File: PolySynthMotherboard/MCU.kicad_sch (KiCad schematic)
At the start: 45 parts, among them J201 SWD Header, J202 USB_C, J203 MIDI_In, J204 MIDI_Thru, J207 MIDI_Out, J401 Micro_SD_Card_Det2, SW201 RST, SW202 BOOT, U201 STM32F411RETx, U202 74HC595, U203 74HC595, U204 4N35, U205 74HC04, Y201 16MHz, Y202 32.768kHZ

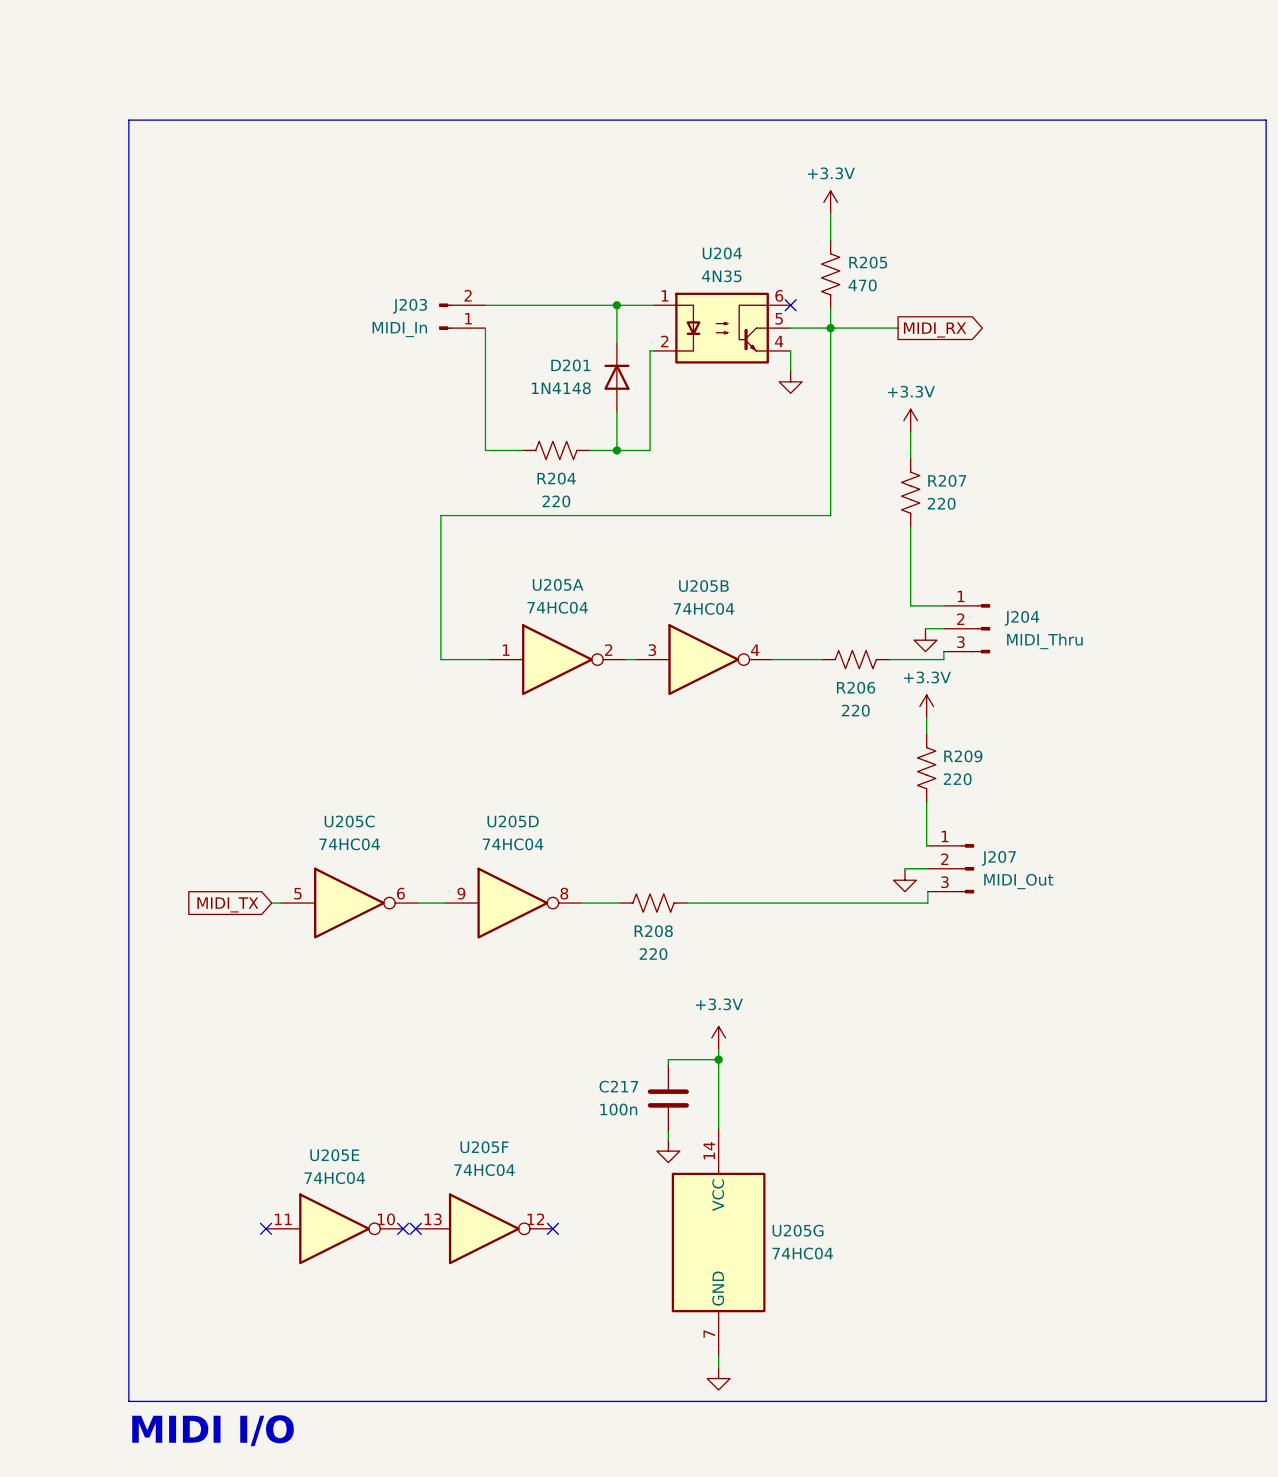
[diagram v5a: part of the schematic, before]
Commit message: fixed footprints, switched optocoupler
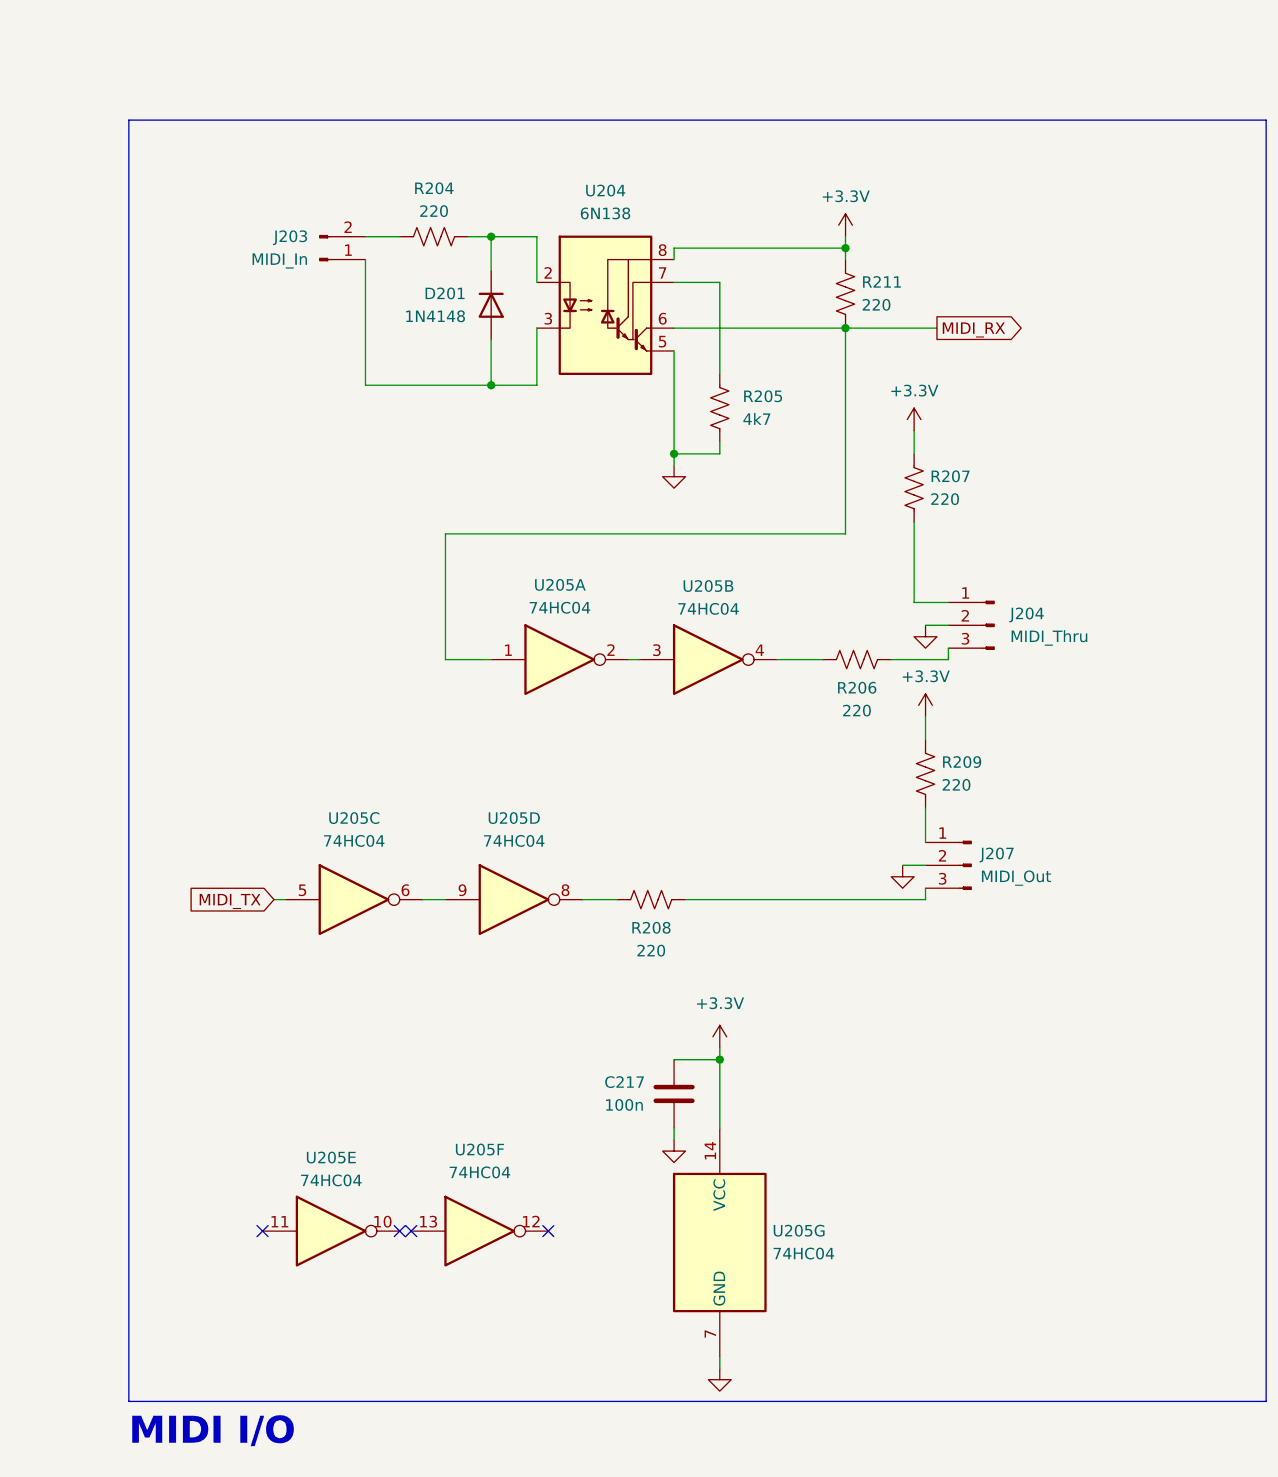
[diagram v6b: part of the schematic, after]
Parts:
- removed U204: 4N35, Package_DIP:DIP-6_W7.62mm, symbol Isolator:4N35
- added R211: 220, Resistor_SMD:R_0805_2012Metric, symbol Device:R_US
- added U204: 6N138, Package_DIP:DIP-8_W7.62mm, symbol Isolator:6N138
- D503: footprint PCM_Diode_SMD_AKL:D_SOD-123 -> Diode_SMD:D_SOD-123
- R201, R202, R203, R204, R206, R207, R208, R209, R404: footprint PCM_Resistor_SMD_AKL:R_0805_2012Metric -> Resistor_SMD:R_0805_2012Metric
- R205: value 470 -> 4k7; footprint PCM_Resistor_SMD_AKL:R_0805_2012Metric -> Resistor_SMD:R_0805_2012Metric
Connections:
- net +3.3V: now also R211.1, U204.8 (VCC); no longer R205.1
- net GND: now also R205.2, U204.5 (GND)
- net MIDI_RX: now also R211.2, U204.6 (VO2); no longer R205.2
- net at D201.1 (K): now also R204.1, U204.2 (C1); no longer J203.2 (Pin_2)
- net at D201.2 (A): now also J203.1 (Pin_1), U204.3 (C2); no longer R204.1
- net at R204.2: now also J203.2 (Pin_2); no longer J203.1 (Pin_1)
- new net: R205.1, U204.7 (VO1)
- no-connect marks 24 -> 23
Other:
- moved on the sheet: C217, D201, J203, J204, R204, R207, R209, U205B, U205C, U205F

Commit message: added terminations
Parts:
- removed D503: PMEG3030, Diode_SMD:D_SOD-123, symbol Device:D_Schottky
- removed J202: USB_C, Connector_USB:USB_C_Receptacle_JAE_DX07S016JA1R1500, symbol Connector:USB_C_Receptacle_USB2.0
- added J202: PWR, Connector_PinHeader_2.54mm:PinHeader_1x05_P2.54mm_Vertical, symbol Connector:Conn_01x05_Pin
- added J205: DATA, Connector_PinHeader_2.54mm:PinHeader_1x03_P2.54mm_Vertical, symbol Connector:Conn_01x03_Pin
- added R212, R213, R214, R215, R216, R217, R218, R219, R220: 22R, Resistor_SMD:R_0805_2012Metric, symbol Device:R_US
- R203: value 4k7 -> 22R
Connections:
- net +3.3V: now also J202.2 (Pin_2)
- net BATT_REF: now also J205.3 (Pin_3)
- net DISP_CS: now also R217.2; no longer U201.50 (PA15)
- net DISP_MOSI: now also R218.1; no longer U201.53 (PC12)
- net DISP_SCK: now also R219.1; no longer U201.51 (PC10)
- net EXP_CS: now also R203.2; no longer U201.33 (PB12)
- net EXP_MOSI: now also R213.2; no longer U201.36 (PB15)
- net EXP_SCK: now also R212.2; no longer U201.34 (PB13)
- net GND: now also J202.1 (Pin_1), J202.5 (Pin_5); no longer R203.2
- net PITCH_MOSI: now also R216.2; no longer U201.23 (PA7)
- net PITCH_SCK: now also R215.2; no longer U201.21 (PA5)
- net PITCH_SS: now also R214.2; no longer U201.20 (PA4)
- net SD_CS: now also R220.1; no longer U201.54 (PD2)
- net USB_D+: now also J205.1 (Pin_1)
- net USB_D-: now also J205.2 (Pin_2)
- net at R203.1: now also U201.33 (PB12)
- new net: R212.1, U201.34 (PB13)
- new net: R216.1, U201.23 (PA7)
- new net: R214.1, U201.20 (PA4)
- new net: R213.1, U201.36 (PB15)
- new net: R215.1, U201.21 (PA5)
- new net: R217.1, U201.50 (PA15)
- new net: R219.2, U201.51 (PC10)
- new net: R218.2, U201.53 (PC12)
- new net: R220.2, U201.54 (PD2)
- new net +12V: J202.3 (Pin_3)
- new net -12V: J202.4 (Pin_4)
- no-connect marks 23 -> 21
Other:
- note added: "Power Input"
- note removed: "USB C Connector"
- moved on the sheet: C208, C209, C211, C212, U202, U203, Y201

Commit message: board iteration
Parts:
- removed R404: 47k, Resistor_SMD:R_0805_2012Metric, symbol Device:R_US
- added R210, R221, R222, R223, R224, R225, R226, R227: 22R, Resistor_SMD:R_0805_2012Metric, symbol Device:R_US
- added R228, R229, R230: 47k, Resistor_SMD:R_0805_2012Metric, symbol Device:R_US
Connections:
- net +3.3V: now also R228.1, R229.1, R230.1
- net DISP_DC: now also R227.2; no longer U201.56 (PB4)
- net DISP_MISO: now also R225.2; no longer J401.7 (DAT0)
- net EXP_CS: now also R230.2
- net PITCH_SS: now also R229.2
- net PIXELS_MAIN: now also R226.2; no longer U201.15 (PA1)
- net PIXELS_MATRIX: now also R210.2; no longer U201.16 (PA2)
- net SD_CS: now also R228.2
- net DAC_A0: no longer names the net of U201.27 (PB1)
- net DAC_A0: now also R222.1
- net DAC_A1: no longer names the net of U201.28 (PB2)
- net DAC_A1: now also R223.1
- net DAC_A2: no longer names the net of U201.29 (PB10)
- net DAC_A2: now also R224.1
- net DAC_INH: no longer names the net of U201.26 (PB0)
- net DAC_INH: now also R221.1
- new net: R226.1, U201.15 (PA1)
- new net: R210.1, U201.16 (PA2)
- new net: R227.1, U201.56 (PB4)
- new net: J401.7 (DAT0), R225.1
- new net MUX_A0: R222.2
- new net MUX_A1: R223.2
- new net MUX_A2: R224.2
- new net MUX_INH: R221.2
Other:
- note added: "CV multiplexer control"
- note added: "Neopixels"
- note added: "Note: not sure if these terminations are necessary but the traces are long so they're here just in case"
- note added: "Port Expander Bus"
- moved on the sheet: C208, C209, C216, C217, D201, J201, J202, J203, J204, J205, J207, J401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
